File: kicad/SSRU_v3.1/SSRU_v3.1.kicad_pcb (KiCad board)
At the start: 2 copper layers, 100 x 100 mm, 119 parts, among them J1 AVR-ISP-6, J11 Conn_01x02, J20 Conn_01x02, J21 Conn_01x02, J22 Conn_01x04, J23 Conn_01x02, J24 Conn_01x04, J25 Conn_01x02, J26 Conn_01x03, J27 Conn_01x03, J3 Conn_01x02, J30 Conn_01x02, J31 Conn_01x04, J32 Conn_01x04, J4 Conn_01x02, J5 Conn_01x02, SW1 SW_Push, U1 MCP2515-xSO, U10 TJA1051T, U11 Ai-Thinker-Ra-02, U12 TJA1051T, U13 CH340N, U14 LM2904, U2 ATmega328P-A, U3 TXS0102DCT, U4 LM2576S-5, U5 AMS1117-3.3, U7 MCP2515-xSO, U8 74LVC1G17, U9 MT3608/SDB628, Y1 16MHz, Y3 16MHz, Y4 16MHz

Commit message: ssru3.1 pcb edgec ut
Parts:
- removed C29, C38, C46: 100nF, RMC_Capacitor:C_0805_2012Metric_Pad1.18x1.45mm_HandSolder_L
- removed C45, C9: 22uF, RMC_Capacitor:C_0805_2012Metric_Pad1.18x1.45mm_HandSolder_L
- removed the G*** at (147.0, 83.8)
- removed the G*** at (150.0, 99.8)
- removed H3, H4: MountingHole, MountingHole:MountingHole_3.2mm_M3
- removed J11, J20, J21, J23, J25, J30: Conn_01x02, Connector_JST:JST_XH_B2B-XH-A_1x02_P2.50mm_Vertical
- removed J22, J24, J32: Conn_01x04, Connector_JST:JST_XH_B4B-XH-A_1x04_P2.50mm_Vertical
- removed J26, J27: Conn_01x03, Connector_JST:JST_XH_B3B-XH-A_1x03_P2.50mm_Vertical
- removed R41: 4k7, RMC_Resistor:R_0805_2012Metric_Pad1.20x1.40mm_HandSolder_L
- removed U3: TXS0102DCT, RMC_SO:SOIC-8_3.9x4.9mm_P1.27mm_RMC_Handsolder
- added C20: 22uF, RMC_Capacitor:C_0805_2012Metric_Pad1.18x1.45mm_HandSolder_L, F.Cu at (252.0, 70.3)
- added J2: Conn_01x24, RMC_Connnector:HD241_24pin, F.Cu at (118.4, 87.9)
- C19: value 100nF -> optional
- C32, C33: footprint RMC_Capacitor:CP_EIA-3528-15_AVX-H_Pad1.50x2.35mm_HandSolder_RMC -> RMC_Capacitor:C_0805_2012Metric_Pad1.18x1.45mm_HandSolder_L
- J1: value AVR-ISP-6 -> Conn_01x03; footprint Connector_PinHeader_2.54mm:PinHeader_2x03_P2.54mm_Vertical -> Connector_PinHeader_2.54mm:PinHeader_1x03_P2.54mm_Vertical
- J3: value Conn_01x02 -> Conn_02x03_Odd_Even; footprint Connector_JST:JST_VH_B2P-VH_1x02_P3.96mm_Vertical -> Connector_PinHeader_2.54mm:PinHeader_2x03_P2.54mm_Vertical
- J4: value Conn_01x02 -> AVR-ISP-6; footprint Connector_JST:JST_XH_B2B-XH-A_1x02_P2.50mm_Vertical -> Connector_PinHeader_2.54mm:PinHeader_2x03_P2.54mm_Vertical
- J5: value Conn_01x02 -> Conn_01x03; footprint Connector_JST:JST_XH_B2B-XH-A_1x02_P2.50mm_Vertical -> Connector_PinHeader_2.54mm:PinHeader_1x03_P2.54mm_Vertical
- L2: footprint Inductor_SMD:L_Wuerth_HCI-5040 -> RMC_Inductor:L_10.4x10.4_H4.8_handsolder
- R1: value 4k7 -> 1M
- R2: value 1k -> 1M
- R3: value 5k -> 1M
- R37: value 100K -> 50k
- R6, R7, R8: value 4.7k -> 1M
- U11: value Ai-Thinker-Ra-02 -> TCA9517D; footprint RF_Module:Ai-Thinker-Ra-01-LoRa -> Package_SO:SOIC-8_3.9x4.9mm_P1.27mm
- moved U14 185.3 mm to (304.3, 79.1), turned to 0 degrees
- moved R24 183.9 mm to (293.4, 81.2), turned to 0 degrees
- moved J31 177.7 mm to (276.4, 67.3)
- moved R25 164.9 mm to (293.4, 84.5), turned to 0 degrees
- moved D6 151.7 mm to (267.9, 75.3), turned to 0 degrees
- moved F3 148.6 mm to (268.9, 99.7), turned to 0 degrees
- moved G*** 146.5 mm to (10.5, 102.7)
- moved J5 145.9 mm to (239.5, 141.3), turned to 0 degrees
- moved U1 144.0 mm to (278.0, 120.8), turned to 0 degrees
- moved SW1 141.3 mm to (250.5, 127.2), turned to 0 degrees
- moved J4 140.5 mm to (244.4, 71.1), turned to 0 degrees
- moved Y1 137.2 mm to (253.7, 87.8), turned to 0 degrees
- moved J1 132.0 mm to (234.9, 141.3)
- moved U7 124.2 mm to (278.0, 128.9), turned to 0 degrees
- moved C33 118.0 mm to (282.5, 111.0)
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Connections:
- C28 pad 1: PUMP_NTC_100k -> PUMP_NTC_50k
- C30 pad 2: +3.3V -> +5V
- J1 pad 1: Net-(J1-MISO) -> PUMP_PWM
- J1 pad 2: +5V -> j3
- J1 pad 3: Net-(J1-SCK) -> GND
- J3 pad 1: +12V -> PUMP_NTC_50k
- J3 pad 2: GND -> FLOW_IN
- J4 pad 1: BRAKE_TEMP1 -> MISO
- J4 pad 2: +24V -> +5V
- J5 pad 1: BRAKE_TEMP2 -> FLOW_OUT
- J5 pad 2: +24V -> FLOW_IN
- R1 pad 1: +3.3V -> GND
- R1 pad 2: LVB_TEMP -> POT1_IN
- R2 pad 1: +12V -> GND
- R2 pad 2: LVB_S -> POT2_IN
- R3 pad 2: LVB_S -> FLOW_IN
- R37 pad 1: PUMP_NTC_100k -> PUMP_NTC_50k
- R40 pad 1: +3.3V -> +5V
- R6 pad 1: MISO -> GND
- R6 pad 2: Net-(J1-MISO) -> PUMP_NTC_50k
- R7 pad 1: MOSI -> GND
- R7 pad 2: Net-(J1-MOSI) -> ENCODER_B
- R8 pad 1: SCK -> GND
- R8 pad 2: Net-(J1-SCK) -> ENCODER_A
- U11 pad 1: GND -> +3.3V
- U11 pad 2: GND -> SCL_3V3
- U11 pad 3: +3.3V -> SDA_3V3
- U11 pad 4: RST -> GND
- U11 pad 5: IRO -> +5V
- U11 pad 6: unconnected-(U11-DIO1-Pad6) -> SDA
- U11 pad 7: unconnected-(U11-DIO2-Pad7) -> SCL
- U11 pad 8: unconnected-(U11-DIO3-Pad8) -> +5V
- U2 pad 1: ENCODER_A -> ENCODER_B
- U2 pad 10: Temp_sensor -> unconnected-(U2-PD6-Pad10)
- U2 pad 11: LVB_TEMP -> DS18B20
- U2 pad 14: CS_CAN3 -> unconnected-(U2-PB2-Pad14)
- U2 pad 2: ENCODER_B -> FLOW_OUT
- U2 pad 25: LVB_S -> unconnected-(U2-PC2-Pad25)
- U2 pad 26: PUMP_NTC_100k -> PUMP_NTC_50k
- U2 pad 32: IRO -> ENCODER_A
- U2 pad 9: FLOW_OUT -> PUMP_PWM
- U8 pad 2: FLOW_IN -> Net-(J5-Pin_3)
- U8 pad 5: +3.3V -> +5V
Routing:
- net +5V: track 434.3 -> 0.00 mm, vias 6 -> 0
- net +3.3V: track 232.5 -> 0.00 mm, vias 5 -> 0
- net RST: track 154.3 -> 0.00 mm, vias 1 -> 0
- net +24V: track 116.3 -> 0.00 mm, vias 1 -> 0
- net MOSI: track 112.2 -> 0.00 mm, vias 6 -> 0
- net SCK: track 112.2 -> 0.00 mm, vias 6 -> 0
- net MISO: track 107.9 -> 0.00 mm, vias 7 -> 0
- net IRO: track 94.9 -> 0.00 mm, vias 4 -> 0
- net LVB_TEMP: track 92.3 -> 0.00 mm, vias 2 -> 0
- net CS_CAN3: track 84.2 -> 0.00 mm, vias 2 -> 0
- net Temp_sensor: track 83.6 -> 0.00 mm, vias 2 -> 0
- net PUMP_NTC_100k: track 77.3 -> 0.00 mm
- net POT1_IN: track 75.0 -> 0.00 mm
- net POT2_IN: track 73.8 -> 0.00 mm, vias 2 -> 0
- net +12V: track 71.5 -> 0.00 mm
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- removed copper zone on B.Cu, net GND
- removed copper zone on F.Cu, net GND
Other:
- board size 100 x 100 mm -> 95 x 78 mm
- board text removed: "+5V"
- board text removed: "+5V MOSI GND"
- board text removed: "12V GND"
- board text removed: "3V3"
- board text removed: "BRK_T1 +24V"
- board text removed: "BRK_T2 +24V"
- board text removed: "GND"
- board text removed: "GND EN_A EN_B +5V"
- board text removed: "GND UD+ UD- +5V"
- board text removed: "H_1 L_1"
- board text removed: "H_2 L_2"
- board text removed: "LVB GND 3V3"
- board text removed: "MISO SCK RST"
- board text removed: "PUMP POT1 POT2 FLOW"
- board text removed: "SCL"
- board text removed: "SDA"
- board text removed: "TEMP GND 3V3"
- board text removed: "USSR v3"

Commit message: SSRU v3.1 updates
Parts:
- removed R30: 5k, RMC_Resistor:R_0805_2012Metric_Pad1.20x1.40mm_HandSolder_L
- removed R31: 1k, RMC_Resistor:R_0805_2012Metric_Pad1.20x1.40mm_HandSolder_L
- added C9: 10uF, RMC_Capacitor:C_0805_2012Metric_Pad1.18x1.45mm_HandSolder_L, F.Cu at (166.0, 68.0)
- added R32: 1k, RMC_Resistor:R_0805_2012Metric_Pad1.20x1.40mm_HandSolder_L, F.Cu at (130.0, 128.0)
- added R33: 22k, RMC_Resistor:R_0805_2012Metric_Pad1.20x1.40mm_HandSolder_L, F.Cu at (127.5, 131.0)
- C12, C15, C16, C19, C30, C6, D2, D6, R3: moved to B.Cu
- J5: footprint Connector_PinHeader_2.54mm:PinHeader_1x03_P2.54mm_Vertical -> Jumper:SolderJumper-3_P1.3mm_Open_Pad1.0x1.5mm
- L2: footprint RMC_Inductor:L_10.4x10.4_H4.8_handsolder -> Inductor_SMD:L_Sunlord_SWPA5040S
- U11: footprint Package_SO:SOIC-8_3.9x4.9mm_P1.27mm -> RMC_SO:SOIC-8_3.9x4.9mm_P1.27mm_RMC_Handsolder
- U13: footprint Package_SO:SOP-8_3.9x4.9mm_P1.27mm -> RMC_SO:SOIC-8_3.9x4.9mm_P1.27mm_RMC_Handsolder
- Y3, Y4: value 16MHz -> 20MHz
- moved C35 223.4 mm to (161.8, -57.6)
- moved R44 221.3 mm to (144.4, -57.6)
- moved C34 220.9 mm to (148.8, -57.6)
- moved U9 216.3 mm to (157.4, -57.5)
- moved C32 209.1 mm to (153.1, -57.6)
- moved R23 209.0 mm to (135.7, -57.6)
- moved C33 204.8 mm to (166.2, -57.6)
- moved U14 190.4 mm to (121.1, 130.8), turned to 180 degrees
- moved R24 182.1 mm to (117.0, 126.5)
- moved D5 181.1 mm to (140.1, -57.6)
- moved R25 174.0 mm to (124.5, 126.5), turned to 180 degrees
- moved L2 168.6 mm to (170.5, -57.5)
- moved U4 158.0 mm to (118.0, 71.0), turned to 180 degrees
- moved C7 150.1 mm to (128.0, 82.0), turned to 180 degrees
- moved L1 139.9 mm to (136.5, 71.0), turned to 90 degrees
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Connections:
- J2 pad 10: POT1_IN -> j1
- J2 pad 11: POT2_IN -> j2
- J2 pad 12: +5V -> j3
- J2 pad 13: DS18B20 -> CAN1-
- J2 pad 14: +24V -> CAN1+
- J2 pad 15: BRAKE_TEMP1 -> CAN2-
- J2 pad 16: BRAKE_TEMP2 -> GND
- J2 pad 18: j1 -> POT1_IN
- J2 pad 19: j2 -> POT2_IN
- J2 pad 2: GND -> +3.3V
- J2 pad 20: j3 -> +5V
- J2 pad 21: +3.3V -> DS18B20
- J2 pad 22: GND -> BRAKE_TEMP1
- J2 pad 23: SCL_3V3 -> BRAKE_TEMP2
- J2 pad 24: SDA_3V3 -> +24V
- J2 pad 3: CAN1- -> SCL_3V3
- J2 pad 4: CAN1+ -> SDA_3V3
- J2 pad 7: CAN2- -> CAN2+
- J2 pad 8: CAN2+ -> GND
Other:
- outline, holes or cut-outs redrawn

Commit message: ssruv3.1
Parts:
- C32, C34: moved to B.Cu
- moved L2 229.2 mm to (104.4, 162.0)
- moved C32 222.9 mm to (96.4, 158.0), turned to -90 degrees
- moved D5 221.3 mm to (112.4, 162.0)
- moved C34 221.3 mm to (98.9, 158.0), turned to 90 degrees
- moved U9 221.0 mm to (104.4, 157.0), turned to 180 degrees
- moved C33 220.7 mm to (114.4, 157.0), turned to 90 degrees
- moved C35 219.2 mm to (116.9, 157.0), turned to -90 degrees
- moved R23 217.0 mm to (110.4, 158.0), turned to 180 degrees
- moved R44 215.8 mm to (110.4, 155.5)
- moved C22 19.5 mm to (131.2, 136.1), turned to 0 degrees
- moved R29 16.4 mm to (126.2, 136.1), turned to 0 degrees
- moved C21 16.0 mm to (133.2, 130.1), turned to 90 degrees
- moved C25 15.5 mm to (131.7, 118.1), turned to 0 degrees
- moved R28 14.6 mm to (128.7, 133.6), turned to 0 degrees
- moved R32 10.6 mm to (126.2, 118.1), turned to 0 degrees
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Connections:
- J2 pad 22: BRAKE_TEMP1 -> +24V
- J2 pad 23: BRAKE_TEMP2 -> BRAKE_TEMP1
- J2 pad 24: +24V -> BRAKE_TEMP2
- J2 pad 9: +5V -> +12V

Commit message: SSRU v3.1 updates
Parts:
- moved C32 42.3 mm to (129.3, 131.4), turned to 90 degrees
- moved C34 38.5 mm to (126.8, 131.4), turned to -90 degrees
- moved L2 38.5 mm to (121.3, 127.4), turned to 180 degrees
- moved D5 34.6 mm to (113.3, 127.4), turned to 180 degrees
- moved U9 29.9 mm to (121.3, 132.4), turned to 0 degrees
- moved R23 27.1 mm to (115.3, 131.4), turned to 0 degrees
- moved C35 25.9 mm to (108.8, 132.4), turned to 90 degrees
- moved C33 24.8 mm to (111.3, 132.4), turned to -90 degrees
- moved R44 22.2 mm to (115.3, 133.9), turned to 180 degrees
- moved U14 8.97 mm to (137.9, 128.1)
- moved R25 8.97 mm to (133.6, 124.7)
- moved R32 8.97 mm to (135.1, 119.2)
- moved R24 8.97 mm to (133.6, 132.2)
- moved R29 8.97 mm to (135.1, 137.2)
- moved C21 8.97 mm to (142.1, 131.2)
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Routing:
- net MOSI: track 0.00 -> 31.3 mm
- net MISO: track 0.00 -> 29.3 mm
- net SCK: track 0.00 -> 26.0 mm, vias 0 -> 2

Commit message: SSRUv3.1
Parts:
- moved G*** 149.6 mm to (158.8, 83.2)
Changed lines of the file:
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@@
 		(locked yes)
 		(layer "F.Cu")
-		(at 10.5 102.7)
+		(at 158.8 83.2)
 		(property "Reference" "G***"
 			(at 0 0 0)

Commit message: TS scheme update
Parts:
- added C23: 100nF, RMC_Capacitor:C_0805_2012Metric_Pad1.18x1.45mm_HandSolder_L, B.Cu at (138.0, 87.0)
- added U3: LM2904, RMC_SO:SOIC-8_3.9x4.9mm_P1.27mm_RMC_Handsolder, F.Cu at (138.0, 86.0)
- C13, C14, C17, C18, C31, C36, C40, C41, C42, C44, C5, R1, R16, R18, R2, R4, R5: moved to B.Cu
- moved R40 100.9 mm to (106.0, 102.0)
- moved G*** 83.3 mm to (241.0, 70.0)
- moved C17 82.0 mm to (187.0, 86.0), turned to -45 degrees
- moved C31 81.2 mm to (137.5, 83.0), turned to -90 degrees
- moved C5 76.3 mm to (193.0, 92.0), turned to 135 degrees
- moved R1 72.8 mm to (135.5, 83.0), turned to -90 degrees
- moved R8 70.8 mm to (124.0, 111.0)
- moved C1 68.0 mm to (203.0, 99.0)
- moved C2 68.0 mm to (203.0, 102.0)
- moved C3 68.0 mm to (203.0, 105.0)
- moved C4 68.0 mm to (203.0, 108.0)
- moved R15 67.4 mm to (159.2, 85.0), turned to 90 degrees
- moved R7 67.1 mm to (124.0, 114.0)
- moved R17 66.6 mm to (148.2, 98.0), turned to -90 degrees
- moved R37 66.0 mm to (138.8, 107.0), turned to 90 degrees
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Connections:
- J2 pad 10: j1 -> CAN1-
- J2 pad 11: j2 -> CAN1+
- J2 pad 12: j3 -> POT2_IN
- J2 pad 13: CAN1- -> j1
- J2 pad 14: CAN1+ -> j2
- J2 pad 15: CAN2- -> j3
- J2 pad 18: POT1_IN -> CAN2-
- J2 pad 19: POT2_IN -> CAN2+
- J2 pad 2: +3.3V -> CAN1-
- J2 pad 3: SCL_3V3 -> CAN1+
- J2 pad 4: SDA_3V3 -> POT1_IN
- J2 pad 5: CAN1- -> +3.3V
- J2 pad 6: CAN1+ -> SCL_3V3
- J2 pad 7: CAN2+ -> SDA_3V3
- R40 pad 2: Temp_sensor -> DS18B20
- U2 pad 19: POT2_IN -> POT2_OUT
- U2 pad 22: POT1_IN -> POT1_OUT
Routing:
- net MOSI: track 31.3 -> 0.00 mm
- net MISO: track 29.3 -> 0.00 mm
- net SCK: track 26.0 -> 0.00 mm, vias 2 -> 0

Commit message: SSRU
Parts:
- added C24: 100nF, RMC_Capacitor:C_0805_2012Metric_Pad1.18x1.45mm_HandSolder_L, B.Cu at (184.0, 132.0)
- added C29: 100nF, RMC_Capacitor:C_0805_2012Metric_Pad1.18x1.45mm_HandSolder_L, B.Cu at (189.0, 76.0)
- added R10: 1M, RMC_Resistor:R_0805_2012Metric_Pad1.20x1.40mm_HandSolder_L, B.Cu at (191.0, 76.0)
- added R9: 1M, RMC_Resistor:R_0805_2012Metric_Pad1.20x1.40mm_HandSolder_L, B.Cu at (184.0, 134.0)
- C13, C14, C19, C23, C30, C31, C32, C34, C36, R1, R2, R3: moved to F.Cu
- C26, C27, C28, C39, C43, R15, R21, R37, R6: moved to B.Cu
- H1, H2: value MountingHole -> MountingHole_Pad; footprint MountingHole:MountingHole_3.2mm_M3 -> MountingHole:MountingHole_3.2mm_M3_ISO14580_Pad
- moved C28 16.7 mm to (143.0, 111.7)
- moved R2 15.3 mm to (128.0, 94.0)
- moved U3 13.9 mm to (131.0, 98.0), turned to 180 degrees
- moved C43 13.0 mm to (165.5, 107.0)
- moved C4 12.2 mm to (193.0, 101.0), turned to 180 degrees
- moved C2 12.2 mm to (193.0, 95.0), turned to 180 degrees
- moved C3 11.7 mm to (193.0, 99.0), turned to 180 degrees
- moved C31 11.5 mm to (134.0, 94.0), turned to 180 degrees
- moved C23 11.0 mm to (137.0, 98.0), turned to 90 degrees
- moved C39 11.0 mm to (165.5, 91.0), turned to 0 degrees
- moved C1 10.2 mm to (193.0, 97.0), turned to 180 degrees
- moved R1 9.12 mm to (134.0, 92.0), turned to 180 degrees
- moved R21 8.97 mm to (165.5, 109.0)
- moved R16 7.98 mm to (165.5, 93.0)
- moved C27 7.74 mm to (158.0, 82.0), turned to 0 degrees
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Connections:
- net 328_RX renamed 328+
- net 328_TX renamed 328-
- U2 pad 12: CS_CAN1 -> unconnected-(U2-PB0-Pad12)
- U2 pad 14: unconnected-(U2-PB2-Pad14) -> CS_CAN1
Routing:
- net MOSI: track 0.00 -> 66.3 mm, vias 0 -> 2
- net MISO: track 0.00 -> 55.1 mm, vias 0 -> 3
- net SCK: track 0.00 -> 55.0 mm, vias 0 -> 2
- net CS_CAN2: track 0.00 -> 37.4 mm, vias 0 -> 2
- net +5V: track 0.00 -> 28.4 mm, vias 0 -> 2
- net 328+: track 0.00 -> 26.9 mm
- net 328-: track 0.00 -> 25.7 mm
- net j1: track 0.00 -> 25.4 mm
- net j3: track 0.00 -> 25.1 mm
- net j2: track 0.00 -> 24.6 mm
- net CS_CAN1: track 0.00 -> 17.9 mm
- net FLOW_IN: track 0.00 -> 14.4 mm
- net UD+: track 0.00 -> 11.8 mm
- net UD-: track 0.00 -> 11.8 mm
- net Net-(U1-OSC2): track 0.00 -> 11.2 mm
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
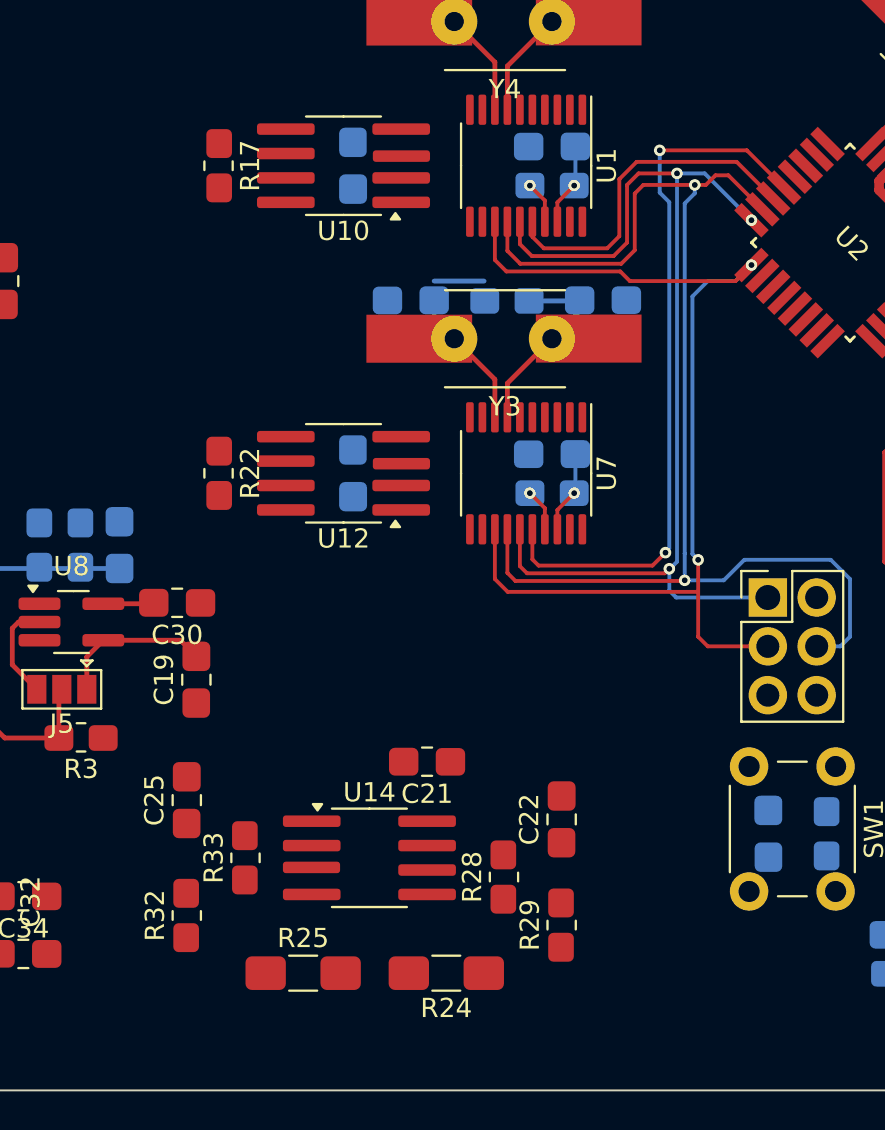
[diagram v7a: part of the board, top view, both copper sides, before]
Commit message: Update PCB layout and backup files
Removed old backup ZIPs and added new ones for SSRU_v3.1. Adjusted component placements and routing in SSRU_v3.1.kicad_pcb, including changes to footprints, coordinates, and net segments for improved layout and connectivity.
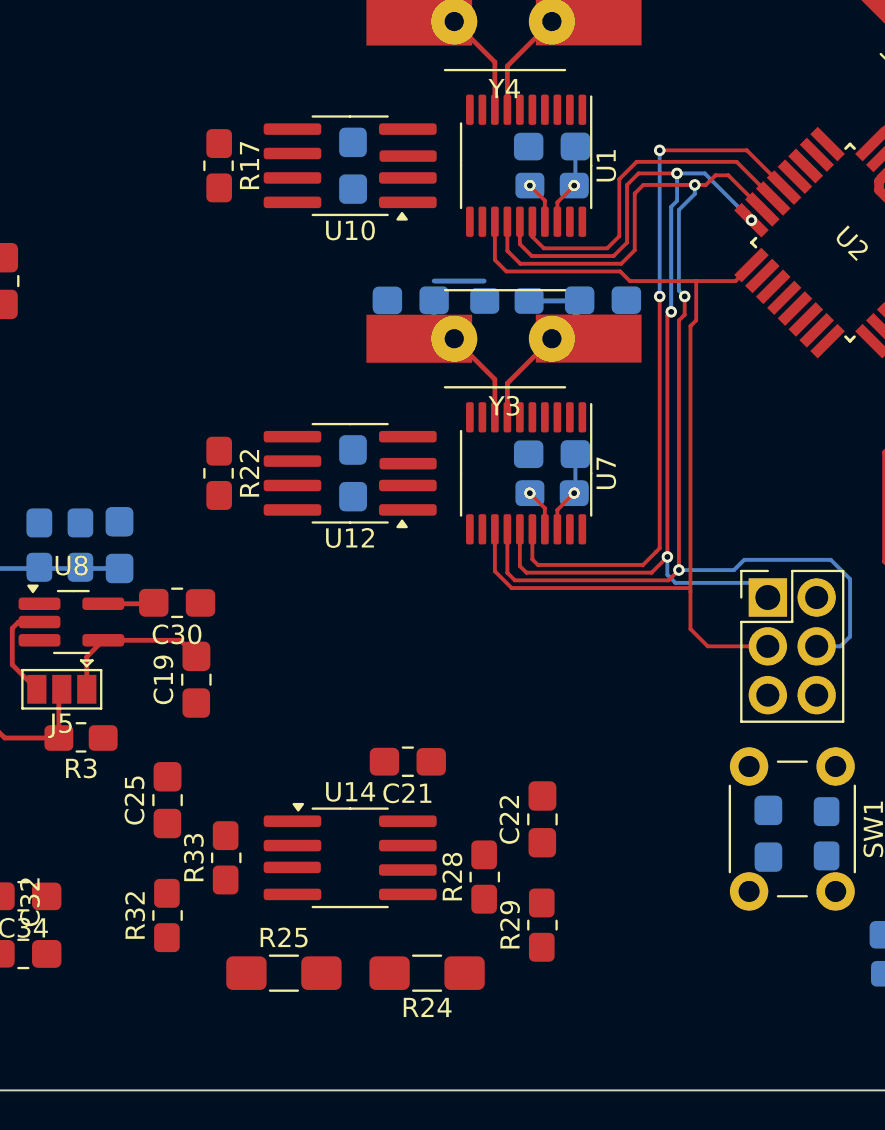
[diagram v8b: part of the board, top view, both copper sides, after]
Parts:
- moved C21 1.00 mm to (158.0, 123.0)
- moved C22 1.00 mm to (165.0, 126.0)
- moved C25 1.00 mm to (145.5, 125.0)
- moved R24 1.00 mm to (159.0, 134.0)
- moved R25 1.00 mm to (151.6, 134.0)
- moved R28 1.00 mm to (162.0, 129.0)
- moved R29 1.00 mm to (165.0, 131.5)
- moved R32 1.00 mm to (145.5, 131.0)
- moved R33 1.00 mm to (148.6, 128.0)
- moved U14 1.00 mm to (155.0, 128.0)
- moved U10 0.35 mm to (155.0, 92.0)
- moved U12 0.35 mm to (155.0, 108.0)
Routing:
- net SCK: track 55.0 -> 51.4 mm, vias 2 -> 0
- net CS_CAN2: track 37.4 -> 36.6 mm
- net MISO: track 55.1 -> 54.9 mm, vias 3 -> 4
- net MOSI: track 66.3 -> 66.1 mm, vias 2 -> 3
